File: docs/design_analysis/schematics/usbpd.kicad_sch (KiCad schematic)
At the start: 27 parts, among them U102 TS3USB221A, U304 CYPD3176

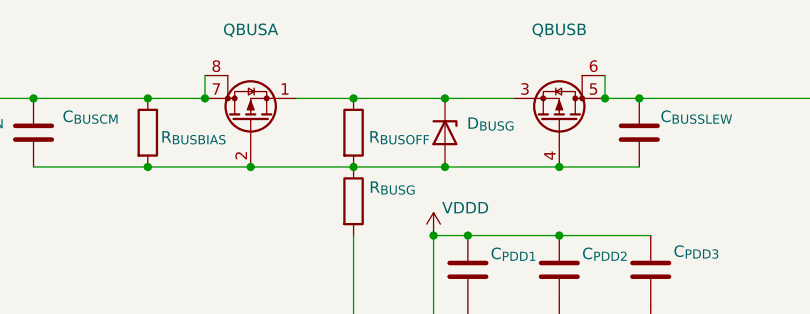
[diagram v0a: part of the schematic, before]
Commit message: HV converter Rev C redesign around LM5156
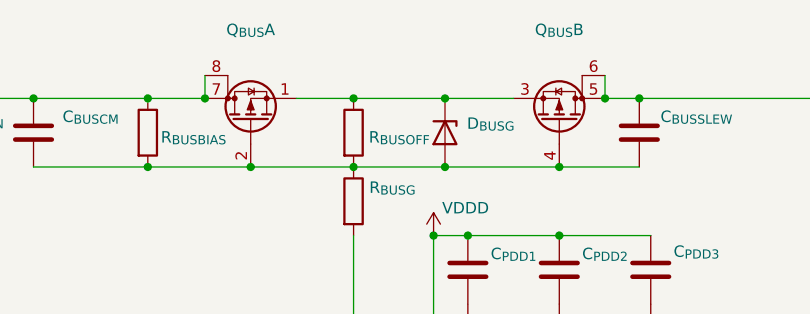
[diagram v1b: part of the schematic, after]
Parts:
- J_{USB}, R_{BUSBLEED}: value ~ -> (none)
- renumbered QBUS to Q_{BUS}
